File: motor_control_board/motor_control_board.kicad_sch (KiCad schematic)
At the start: 36 parts, among them J1 Conn_01x05_Female, J2 Conn_01x05_Female, J3 Harwin_G125-MG10605M4P, J4 Harwin_M80-5000000M5-02-333-0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, J5 Harwin_M80-5400642, J6 Harwin_M80-8510442, J7 Harwin_M80-8510442, U1 CPC1117N

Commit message: Free some Real estate so Joe can move in
Moved things around, generate production files
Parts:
- removed J1, J2: Conn_01x05_Female, canhw_footprints:PinSocket_5x2.54_SMD_90deg_952-3198-1-ND, symbol canhw:Conn_01x05_Socket
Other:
- added sheet Programming Header (header.kicad_sch)
- note removed: "FS Programming Header"
- note removed: "MCU Programming Header"
- moved on the sheet: C1, C16, C17, C18, C19, C21, D1, D2, D3, D4, D9, F1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

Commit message: Fix DRC warnings
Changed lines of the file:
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@@
 	)
 	(junction
-		(at 106.045 107.315)
-		(diameter 0)
-		(color 0 0 0 0)
-	)
-	(junction
 		(at 238.76 142.24)
 		(diameter 0)
@@
 	(wire
 		(pts
-			(xy 106.045 104.14) (xy 106.045 107.315)
-		)
-		(stroke
-			(width 0)
-			(type default)
-		)
-	)
-	(wire
-		(pts
 			(xy 54.61 167.64) (xy 60.96 167.64)
 		)
@@
 					(unit 1)
 				)
-			)
-		)
-	)
-	(symbol
-		(lib_id "canhw:PWR_FLAG")
-		(at 106.045 104.14 0)
-		(unit 1)
-		(exclude_from_sim no)
-		(in_bom yes)
-		(on_board yes)
-		(dnp no)
-		(fields_autoplaced yes)
-		(property "Reference" "#FLG02"
-			(at 106.045 102.235 0)
-			(effects
-				(font
-					(size 1.27 1.27)
-				)
-				(hide yes)
-			)
-		)
-		(property "Value" "PWR_FLAG"
-			(at 106.045 99.695 0)
-			(effects
-				(font
-					(size 1.27 1.27)
-				)
-			)
-		)
-		(property "Footprint" ""
-			(at 106.045 104.14 0)
-			(effects
-				(font
-					(size 1.27 1.27)
-				)
-				(hide yes)
-			)
-		)
-		(property "Datasheet" "~"
-			(at 106.045 104.14 0)
-			(effects
-				(font
-					(size 1.27 1.27)
-				)
-				(hide yes)
-			)
-		)
-		(property "Description" "Special symbol for telling ERC where power comes from"
-			(at 106.045 104.14 0)
-			(effects
-				(font
-					(size 1.27 1.27)
-				)
-				(hide yes)
-			)
-		)
-		(pin "1"
-		)
-		(instances
-			(project ""
-				(path "/ced26b11-410b-4897-bfe1-68b095b3fef4"
-					(reference "#FLG02")
-					(unit 1)
-				)

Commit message: skill issued two pinouts
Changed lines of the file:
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@@
 	(wire
 		(pts
-			(xy 106.68 54.61) (xy 106.68 80.01)
-		)
-		(stroke
-			(width 0)
-			(type default)
-		)
-	)
-	(wire
-		(pts
 			(xy 168.275 84.455) (xy 168.275 78.105)
 		)
@@
 	(wire
 		(pts
+			(xy 102.87 74.93) (xy 102.87 49.53)
+		)
+		(stroke
+			(width 0)
+			(type default)
+		)
+	)
+	(wire
+		(pts
 			(xy 250.19 113.665) (xy 250.19 113.03)
 		)
@@
 	(wire
 		(pts
-			(xy 101.6 49.53) (xy 114.3 49.53)
-		)
-		(stroke
-			(width 0)
-			(type default)
-		)
-	)
-	(wire
-		(pts
 			(xy 168.275 92.075) (xy 168.275 96.52)
 		)
@@
 	(wire
 		(pts
-			(xy 101.6 74.93) (xy 101.6 49.53)
+			(xy 16.51 29.21) (xy 39.37 29.21)
 		)
 		(stroke
@@
 	(wire
 		(pts
-			(xy 16.51 29.21) (xy 39.37 29.21)
+			(xy 252.73 139.7) (xy 252.73 142.24)
 		)
 		(stroke
@@
 	(wire
 		(pts
-			(xy 252.73 139.7) (xy 252.73 142.24)
+			(xy 108.585 129.54) (xy 116.84 129.54)
 		)
 		(stroke
@@
 	(wire
 		(pts
-			(xy 108.585 129.54) (xy 116.84 129.54)
+			(xy 39.37 114.3) (xy 39.37 116.84)
 		)
 		(stroke
@@
 	(wire
 		(pts
-			(xy 39.37 114.3) (xy 39.37 116.84)
+			(xy 78.74 69.85) (xy 96.52 69.85)
 		)
 		(stroke
@@
 	(wire
 		(pts
-			(xy 78.74 69.85) (xy 96.52 69.85)
+			(xy 168.275 96.52) (xy 168.275 98.425)
 		)
 		(stroke
@@
 	(wire
 		(pts
-			(xy 168.275 96.52) (xy 168.275 98.425)
+			(xy 78.74 74.93) (xy 102.87 74.93)
+		)
+		(stroke
+			(width 0)
+			(type default)
+		)
+	)
+	(wire
+		(pts
+			(xy 102.87 49.53) (xy 114.3 49.53)
 		)
 		(stroke
@@
 	(wire
 		(pts
-			(xy 78.74 74.93) (xy 101.6 74.93)
+			(xy 78.74 80.01) (xy 106.68 80.01)
 		)
 		(stroke
@@
 	(wire
 		(pts
+			(xy 106.68 80.01) (xy 106.68 54.61)
+		)
+		(stroke
+			(width 0)
+			(type default)
+		)
+	)
+	(wire
+		(pts
 			(xy 71.755 119.38) (xy 82.55 119.38)
 		)
@@
 	(wire
 		(pts
-			(xy 106.68 80.01) (xy 78.74 80.01)
-		)
-		(stroke
-			(width 0)
-			(type default)
-		)
-	)
-	(wire
-		(pts
 			(xy 158.75 92.075) (xy 158.75 96.52)
 		)
@@
 		)
 		(pin "ICSPDAT_FS" bidirectional
-			(at 78.74 74.93 0)
+			(at 78.74 80.01 0)
 			(effects
 				(font
@@
 		)
 		(pin "ICSPCLK_FS" output
-			(at 78.74 80.01 0)
+			(at 78.74 74.93 0)
 			(effects
 				(font

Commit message: addressed concerns
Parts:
- added C20: 22u, Capacitor_SMD:C_0805_2012Metric_Pad1.18x1.45mm_HandSolder, symbol canhw:C
- J4: footprint canhw_footprints:HARWIN_M80-5000000M5-02-333-00-000 -> canhw_footprints:TE_2-1437667-4
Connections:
- net Batt+: now also J4.2 (Pin_2), C20.1; no longer J4.1 (Pin_1)
- net GND: now also J4.1 (Pin_1), C20.2; no longer J4.2 (Pin_2)
- net ENC1_IN: no longer names the net of J6.2 (Pin_2), R1.1
- net ENC2_IN: no longer names the net of J7.2 (Pin_2), R4.1
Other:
- moved on the sheet: C18, C19

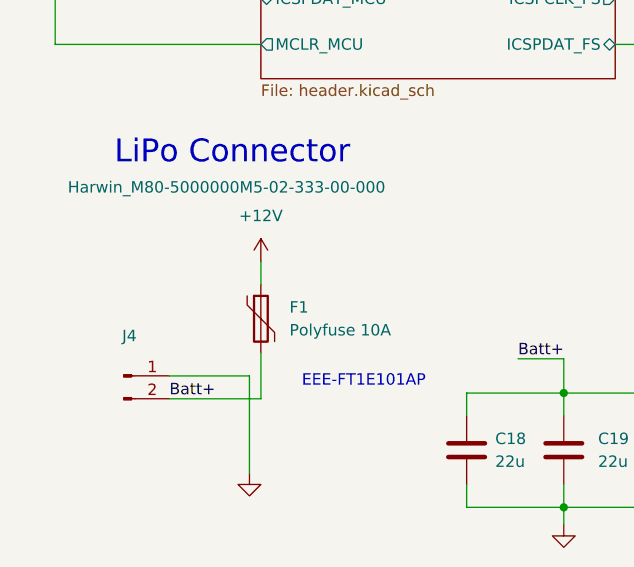
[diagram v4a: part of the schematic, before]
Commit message: minor schematic and copper pour cleanup
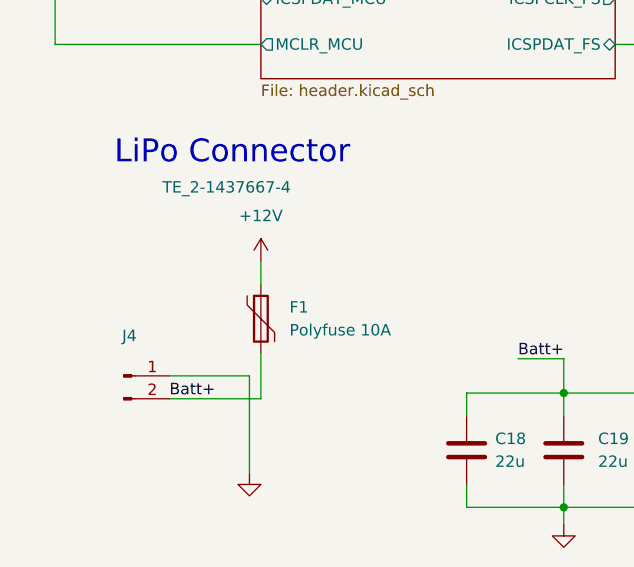
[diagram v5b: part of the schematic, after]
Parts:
- J4: value Harwin_M80-5000000M5-02-333-00-000 -> TE_2-1437667-4
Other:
- note removed: "EEE-FT1E101AP"
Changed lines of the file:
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@@
-		)
-	)
-	(text "EEE-FT1E101AP\n"
-		(exclude_from_sim no)
-		(at 50.8 117.475 0)
-		(effects
-			(font
-				(size 1.27 1.27)
-			)
 		)
 	)
@@
 			)
 		)
-		(property "Value" "Harwin_M80-5000000M5-02-333-00-000"
+		(property "Value" "TE_2-1437667-4"
 			(at 35.56 95.885 0)
 			(effects
